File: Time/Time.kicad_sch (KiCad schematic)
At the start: 10 parts, among them J1 Buss, SW1 Slot, U1 DS12885, U2 74LS573, U3 74LS245, U4 GAL22V10, U5 74LS85, Y1 32.768KHz/6pF

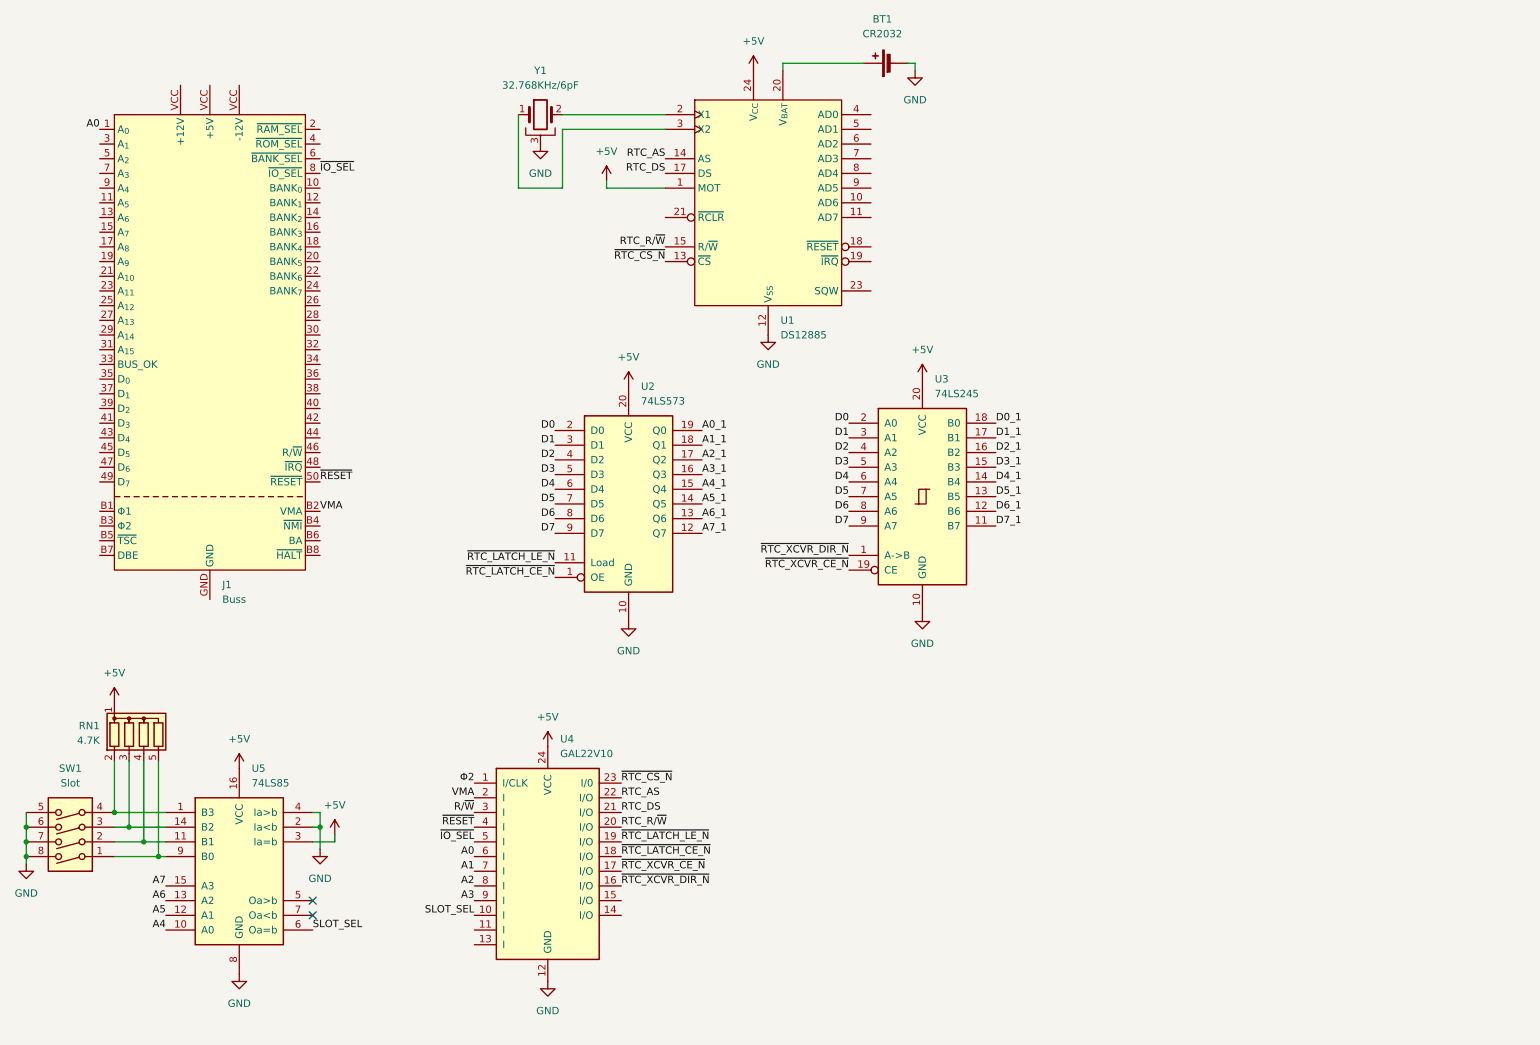
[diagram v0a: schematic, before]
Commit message: finish layout on time board. still need to verify RTC's multiplexed IO
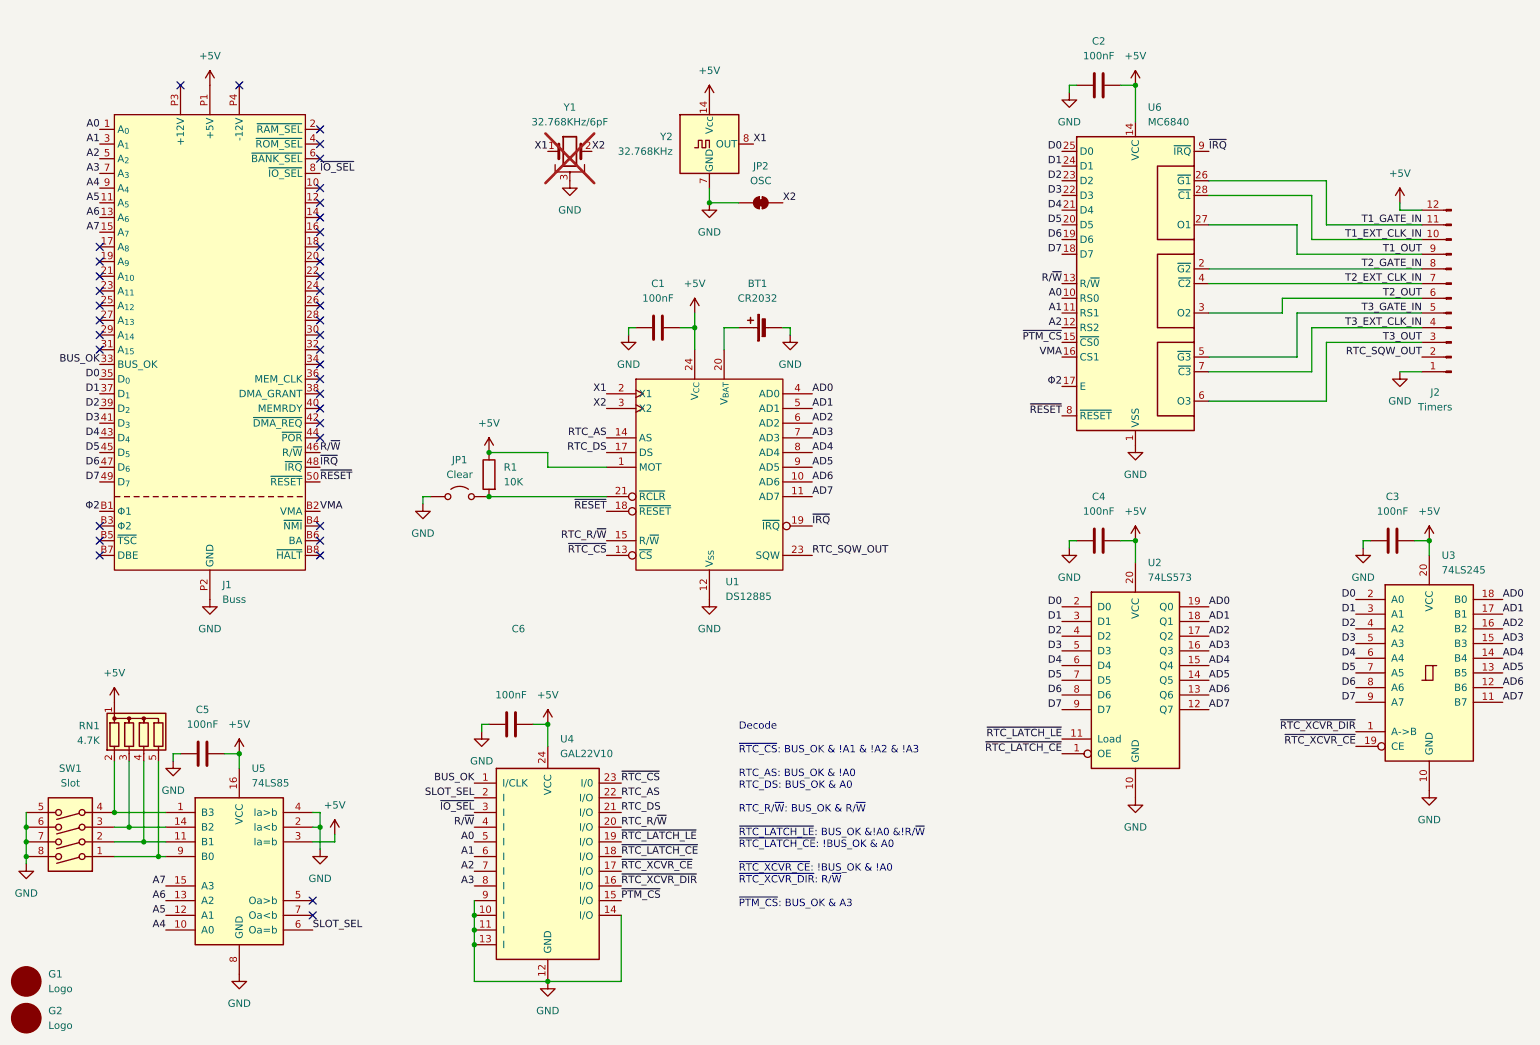
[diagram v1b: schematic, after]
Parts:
- added C1, C2, C3, C4, C5, C6: 100nF, 0-Footprints:C_Disc_D5.0mm_W2.5mm_P5.00mm, symbol Device:C
- added G1: Logo, 0-Footprints:Crank, symbol 0-Symbols:Logo
- added G2: Logo, 0-Footprints:crankery_small, symbol 0-Symbols:Logo
- added J2: Timers, 0-Footprints:PinHeader_1x12_P2.54mm_Horizontal, symbol Connector:Conn_01x12_Pin
- added JP1: Clear, Connector_PinHeader_2.54mm:PinHeader_1x02_P2.54mm_Horizontal, symbol Jumper:Jumper_2_Open
- added JP2: OSC, 0-Footprints:SolderJumper-2_P1.3mm_Bridged_RoundedPad1.0x1.5mm, symbol Jumper:SolderJumper_2_Bridged
- added R1: 10K, 0-Footprints:R_Axial_DIN0204_L3.6mm_D1.6mm_P7.62mm_Horizontal, symbol Device:R
- added U6: MC6840, 0-Footprints:DIP-28_W15.24mm, symbol Interface:MC6840
- added Y2: 32.768KHz, 0-Footprints:Oscillator_DIP-14, symbol Oscillator:DGOF5S3
- BT1: footprint (none) -> Battery:BatteryHolder_Keystone_1060_1x2032
- J1: footprint (none) -> 0-Footprints:Card
- RN1: footprint Resistor_THT:R_Array_SIP5 -> 0-Footprints:R_Array_SIP5
- SW1: footprint (none) -> 0-Footprints:SW_DIP_SPSTx04_Slide_9.78x12.34mm_W7.62mm_P2.54mm
- U1: footprint Package_SO:SOIC-24W_7.5x15.4mm_P1.27mm -> 0-Footprints:DIP-24_W15.24mm
- U2, U3: footprint (none) -> 0-Footprints:DIP-20_W7.62mm
- U4: footprint Package_DIP:DIP-24_W7.62mm -> 0-Footprints:DIP-24_W7.62mm
- U5: footprint (none) -> 0-Footprints:DIP-16_W7.62mm
- Y1: footprint (none) -> 0-Footprints:Crystal_AT310_D3.0mm_L10.0mm_Horizontal_1EP_style2; now not fitted
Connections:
- net A0_1 is gone; now on net AD0: U2.19 (Q0)
- net A1_1 is gone; now on net AD1: U2.18 (Q1)
- net A2_1 is gone; now on net AD2: U2.17 (Q2)
- net A3_1 is gone; now on net AD3: U2.16 (Q3)
- net A4_1 is gone; now on net AD4: U2.15 (Q4)
- net A5_1 is gone; now on net AD5: U2.14 (Q5)
- net A6_1 is gone; now on net AD6: U2.13 (Q6)
- net A7_1 is gone; now on net AD7: U2.12 (Q7)
- net D0_1 is gone; now on net AD0: U3.18 (B0)
- net D1_1 is gone; now on net AD1: U3.17 (B1)
- net D2_1 is gone; now on net AD2: U3.16 (B2)
- net D3_1 is gone; now on net AD3: U3.15 (B3)
- net D4_1 is gone; now on net AD4: U3.14 (B4)
- net D5_1 is gone; now on net AD5: U3.13 (B5)
- net D6_1 is gone; now on net AD6: U3.12 (B6)
- net D7_1 is gone; now on net AD7: U3.11 (B7)
- net +5V: now also J1.P1 (+5V), C1.2, C2.2, C3.2, C4.2, C5.2, C6.2, J2.12 (Pin_12), R1.1, U6.14 (VCC), Y2.14 (Vcc)
- net A0: now also U4.5 (I), U6.10 (RS0); no longer U4.6 (I)
- net A1: now also J1.3 (A_{1}), U4.6 (I), U6.11 (RS1); no longer U4.7 (I)
- net A2: now also J1.5 (A_{2}), U4.7 (I), U6.12 (RS2); no longer U4.8 (I)
- net A3: now also J1.7 (A_{3}), U4.8 (I); no longer U4.9 (I)
- net A4: now also J1.9 (A_{4})
- net A5: now also J1.11 (A_{5})
- net A6: now also J1.13 (A_{6})
- net A7: now also J1.15 (A_{7})
- net D0: now also J1.35 (D_{0}), U6.25 (D0)
- net D1: now also J1.37 (D_{1}), U6.24 (D1)
- net D2: now also J1.39 (D_{2}), U6.23 (D2)
- net D3: now also J1.41 (D_{3}), U6.22 (D3)
- net D4: now also J1.43 (D_{4}), U6.21 (D4)
- net D5: now also J1.45 (D_{5}), U6.20 (D5)
- net D6: now also J1.47 (D_{6}), U6.19 (D6)
- net D7: now also J1.49 (D_{7}), U6.18 (D7)
- net GND: now also J1.P2 (GND), U4.10 (I), U4.11 (I), U4.13 (I), U4.14 (I/O), U4.9 (I), C1.1, C2.1, C3.1, C4.1, C5.1, C6.1, J2.1 (Pin_1), JP1.1 (A), JP2.1 (A), U6.1 (VSS), Y2.7 (GND)
- net R/~{W}: now also J1.46 (R/~{W}), U4.4 (I), U6.13 (R/~{W}); no longer U4.3 (I)
- net SLOT_SEL: now also U4.2 (I); no longer U4.10 (I)
- net VMA: now also U6.16 (CS1); no longer U4.2 (I)
- net ~{IO_SEL}: now also U4.3 (I); no longer U4.5 (I)
- net ~{RESET}: now also U1.18 (~{RESET}), U6.8 (~{RESET}); no longer U4.4 (I)
- net Φ2: now also J1.B1 (Φ1), U6.17 (E); no longer U4.1 (I/CLK)
- net X1: now reaches Y1.1
- net X1: now also U1.2 (X1), Y2.8 (OUT); no longer U1.3 (X2)
- net X2: now reaches Y1.2
- net X2: now also U1.3 (X2), JP2.2 (B); no longer U1.2 (X1)
- net BUS_OK: now reaches J1.33 (BUS_OK)
- net BUS_OK: now also U4.1 (I/CLK)
- net ~{IRQ}: now reaches J1.48 (~{IRQ})
- net ~{IRQ}: now also U1.19 (~{IRQ}), U6.9 (~{IRQ})
- net AD6: now reaches U1.10 (AD6)
- net AD7: now reaches U1.11 (AD7)
- net at U1.21 (~{RCLR}): now also JP1.2 (B), R1.2
- net RTC_SQW_OUT: now reaches U1.23 (SQW)
- net RTC_SQW_OUT: now also J2.2 (Pin_2)
- net AD0: now reaches U1.4 (AD0)
- net AD1: now reaches U1.5 (AD1)
- net AD2: now reaches U1.6 (AD2)
- net AD3: now reaches U1.7 (AD3)
- net AD4: now reaches U1.8 (AD4)
- net AD5: now reaches U1.9 (AD5)
- net ~{PTM_CS}: now reaches U4.15 (I/O)
- net ~{PTM_CS}: now also U6.15 (~{CS0})
- net ~{RTC_CS_N} renamed ~{RTC_CS}
- net ~{RTC_LATCH_CE_N} renamed ~{RTC_LATCH_CE}
- net ~{RTC_LATCH_LE_N} renamed ~{RTC_LATCH_LE}
- net ~{RTC_XCVR_CE_N} renamed ~{RTC_XCVR_CE}
- net ~{RTC_XCVR_DIR_N} renamed ~{RTC_XCVR_DIR}
- new net T1_EXT_CLK_IN: J2.10 (Pin_10), U6.28 (~{C1})
- new net T1_GATE_IN: J2.11 (Pin_11), U6.26 (~{G1})
- new net T1_OUT: J2.9 (Pin_9), U6.27 (O1)
- new net T2_EXT_CLK_IN: J2.7 (Pin_7), U6.4 (~{C2})
- new net T2_GATE_IN: J2.8 (Pin_8), U6.2 (~{G2})
- new net T2_OUT: J2.6 (Pin_6), U6.3 (O2)
- new net T3_EXT_CLK_IN: J2.4 (Pin_4), U6.7 (~{C3})
- new net T3_GATE_IN: J2.5 (Pin_5), U6.5 (~{G3})
- new net T3_OUT: J2.3 (Pin_3), U6.6 (O3)
- no-connect marks 2 -> 39
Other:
- note added: "Decode ~{RTC_CS}: BUS_OK & !A1 & !A2 & !A3 RTC_AS: BUS_OK & !A0 RTC_DS: BUS_OK & A0 RTC_R/~{W}: BUS_OK & R/~{W} ~{RTC_LATCH_LE}: BUS_OK &!A0 &!R/~{W} ~{RTC_LATCH_CE}: !BUS_OK & A0 ~{RTC_XCVR_CE}: !BUS_OK & !A0 ~{RTC_XCVR_DIR}: R/~{W} ~{PTM_CS}: BUS_OK & A3"
- moved on the sheet: BT1, U1, U2, U3

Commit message: finish routing the coms board. add some step models to look at this thing in freecad
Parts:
- BT1: footprint Battery:BatteryHolder_Keystone_1060_1x2032 -> 0-Footprints:BatteryHolder_Keystone_1060_1x2032
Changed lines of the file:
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@@
 			)
 		)
-		(property "Footprint" "Battery:BatteryHolder_Keystone_1060_1x2032"
+		(property "Footprint" "0-Footprints:BatteryHolder_Keystone_1060_1x2032"
 			(at 149.606 71.12 90)
 			(effects

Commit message: ugh. resetting...
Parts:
- removed RN1: 4.7K, 0-Footprints:R_Array_SIP5, symbol Device:R_Network04
- removed SW1: Slot, 0-Footprints:SW_DIP_SPSTx04_Slide_9.78x12.34mm_W7.62mm_P2.54mm, symbol Switch:SW_DIP_x04
- removed U5: 74LS85, 0-Footprints:DIP-16_W7.62mm, symbol 74xx:74LS85
- added C7: 100nF, 0-Footprints:C_Disc_D5.0mm_W2.5mm_P5.00mm, symbol Device:C
- added J3: Parallel, 0-Footprints:PinHeader_1x12_P2.54mm_Horizontal, symbol Connector:Conn_01x12_Pin
- added U7: MC6821, 0-Footprints:DIP-40_W15.24mm, symbol Interface:6821
- added U8: ATtiny85, 0-Footprints:DIP-8_W7.62mm, symbol MCU_Microchip_ATtiny:ATtiny85-20P
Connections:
- net SLOT_SEL is gone; now on net ~{IO_SEL}: U4.2 (I)
- net +5V: now also C7.2, J3.1 (Pin_1), U7.20 (VCC), U8.8 (VCC)
- net A0: now also U4.3 (I), U7.36 (RS0); no longer U4.5 (I)
- net A1: now also U4.4 (I), U7.35 (RS1); no longer U4.6 (I)
- net A2: now also U4.5 (I); no longer U4.7 (I)
- net A3: now also U4.6 (I); no longer U4.8 (I)
- net A4: now also U4.7 (I)
- net A5: now also U4.8 (I)
- net A6: now also U4.9 (I)
- net A7: now also U4.10 (I)
- net D0: now also U7.33 (D0)
- net D1: now also U7.32 (D1)
- net D2: now also U7.31 (D2)
- net D3: now also U7.30 (D3)
- net D4: now also U7.29 (D4)
- net D5: now also U7.28 (D5)
- net D6: now also U7.27 (D6)
- net D7: now also U7.26 (D7)
- net GND: now also U1.13 (~{CS}), U4.15 (I/O), U4.16 (I/O), U4.17 (I/O), U4.18 (I/O), C7.1, J3.12 (Pin_12), U7.1 (VSS), U8.4 (GND); no longer U4.10 (I), U4.11 (I), U4.9 (I)
- net R/~{W}: now also U1.15 (R/~{W}), U4.11 (I), U7.21 (R/~{W}); no longer U4.4 (I)
- net VMA: now also U7.24 (CS1)
- net ~{IO_SEL}: no longer U4.3 (I)
- net ~{IRQ}: now also U7.37 (~{IRQB}), U7.38 (~{IRQA})
- net ~{PTM_CS}: no longer U4.15 (I/O)
- net ~{RESET}: now also U7.34 (~{RESET})
- net Φ2: now also U7.25 (ENABLE)
- net RTC_AS renamed ~{RTC_ADDR_SEL}
- net ~{RTC_ADDR_SEL}: now also U2.1 (OE), U2.11 (Load), U4.23 (I/0); no longer U4.22 (I/O)
- net RTC_DS renamed ~{PTM_SEL}
- net ~{PTM_SEL}: no longer U1.17 (DS)
- net RTC_R/~{W} renamed ~{PIA_SEL}
- net ~{PIA_SEL}: no longer U1.15 (R/~{W})
- removed net ~{RTC_CS}: U1.13 (~{CS}), U4.23 (I/0)
- removed net ~{RTC_LATCH_CE}: U2.1 (OE), U4.18 (I/O)
- net ~{RTC_LATCH_LE} renamed W/~{R}
- net W/~{R}: now also U3.1 (A->B); no longer U2.11 (Load)
- net ~{RTC_XCVR_CE} renamed ~{RTC_DATA_SEL}
- net ~{RTC_DATA_SEL}: now also U1.17 (DS), U4.22 (I/O); no longer U4.17 (I/O)
- removed net ~{RTC_XCVR_DIR}: U3.1 (A->B), U4.16 (I/O)
- new net: U7.10 (PB0), U8.5 (AREF/PB0)
- new net: U7.11 (PB1), U8.6 (PB1)
- new net: U7.12 (PB2), U8.7 (PB2)
- new net: U7.13 (PB3), U8.2 (XTAL1/PB3)
- new net: U7.18 (CB1), U8.3 (XTAL2/PB4)
- new net: J3.2 (Pin_2), U7.2 (PA0)
- new net: J3.3 (Pin_3), U7.3 (PA1)
- new net: J3.11 (Pin_11), U7.39 (CA2)
- new net: J3.4 (Pin_4), U7.4 (PA2)
- new net: J3.10 (Pin_10), U7.40 (CA1)
- new net: J3.5 (Pin_5), U7.5 (PA3)
- new net: J3.6 (Pin_6), U7.6 (PA4)
- new net: J3.7 (Pin_7), U7.7 (PA5)
- new net: J3.8 (Pin_8), U7.8 (PA6)
- new net: J3.9 (Pin_9), U7.9 (PA7)
- new net ~{PIA_CS}: U7.23 (~{CS2})
- no-connect marks 39 -> 42
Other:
- note added: "Decode: * Slot is currently fixed at 0x4. * All outputs inculde "GLOBAL". W/~{R}: !R/~{W} GLOBAL: BUS_OK & !A7 & !A6 & A5 & !A4 ~{RTC_ADDR_SEL}: GLOBAL & !A3 & !A2 & !A1 & !A0 ~{RTC_DATA_SEL}: GLOBAL & !A3 & !A2 & !A1 & A0 ~{PIA_SEL}: GLOBAL & !A3 & A2 ~{PTM_SEL}: GLOBAL & A3"
- note added: "Memory Map (0x40-0x4F) 0b0000 0x40: RTC addr 0b0001 0x41: RTC data 0b0010 0x42: free 0b0011 0x43: free 0b0100 0x44: PIA 0b0101 0x45: PIA 0b0110 0x46: PIA 0b0111 0x47: PIA 0b1000 0x48: PTC 0b1001 0x49: PTC 0b1010 0x4a: PTC 0b1011 0x4b: PTC 0b1100 0x4c: PTC 0b1101 0x4d: PTC 0b1110 0x4e: PTC 0b1111 0x4f: PTC"
- note removed: "Decode ~{RTC_CS}: BUS_OK & !A1 & !A2 & !A3 RTC_AS: BUS_OK & !A0 RTC_DS: BUS_OK & A0 RTC_R/~{W}: BUS_OK & R/~{W} ~{RTC_LATCH_LE}: BUS_OK &!A0 &!R/~{W} ~{RTC_LATCH_CE}: !BUS_OK & A0 ~{RTC_XCVR_CE}: !BUS_OK & !A0 ~{RTC_XCVR_DIR}: R/~{W} ~{PTM_CS}: BUS_OK & A3"
- moved on the sheet: BT1, C1, C2, C3, C4, C6, G1, G2, J2, JP1, R1, U1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

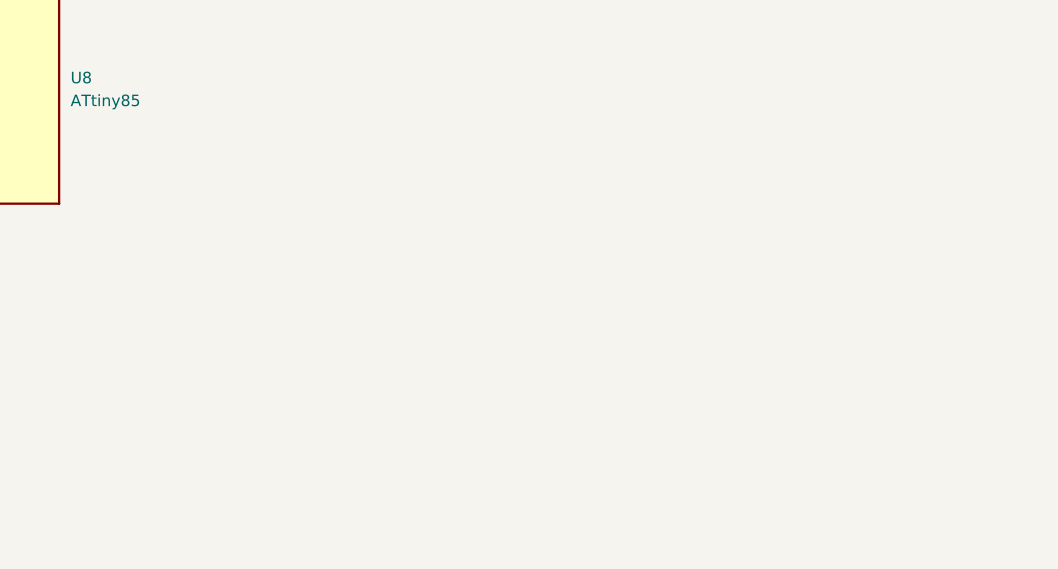
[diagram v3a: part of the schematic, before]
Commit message: start moving towards helper methods on the cpu operations
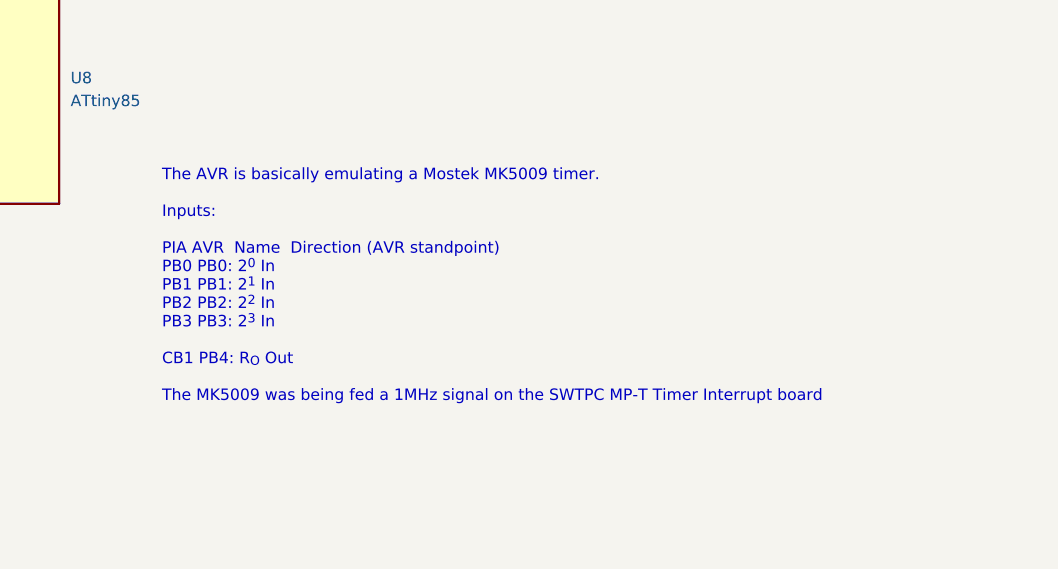
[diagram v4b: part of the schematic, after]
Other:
- note added: "The AVR is basically emulating a Mostek MK5009 timer. Inputs: PIA AVR Name Direction (AVR standpoint) PB0 PB0: 2^{0} In PB1 PB1: 2^{1} In PB2 PB2: 2^{2} In PB3 PB3: 2^{3} In CB1 PB4: R_{O} Out The MK5009 was being fed a 1MHz signal on the SWTPC MP-T Timer Interrupt board"
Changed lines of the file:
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@@
+		)
+	)
+	(text "The AVR is basically emulating a Mostek MK5009 timer.\n\nInputs:\n\nPIA AVR  Name  Direction (AVR standpoint)\nPB0 PB0: 2^{0} In\nPB1 PB1: 2^{1} In\nPB2 PB2: 2^{2} In\nPB3 PB3: 2^{3} In\n\nCB1 PB4: R_{O} Out\n\nThe MK5009 was being fed a 1MHz signal on the SWTPC MP-T Timer Interrupt board"
+		(exclude_from_sim no)
+		(at 321.31 93.98 0)
+		(effects
+			(font
+				(face "Courier")
+				(size 1.27 1.27)
+			)
+			(justify left top)
 		)
 	)
